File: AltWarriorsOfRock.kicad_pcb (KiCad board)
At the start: 2 copper layers, 35 x 90.5 mm, 17 parts, among them J1 Fret Board, J2 South Inputs

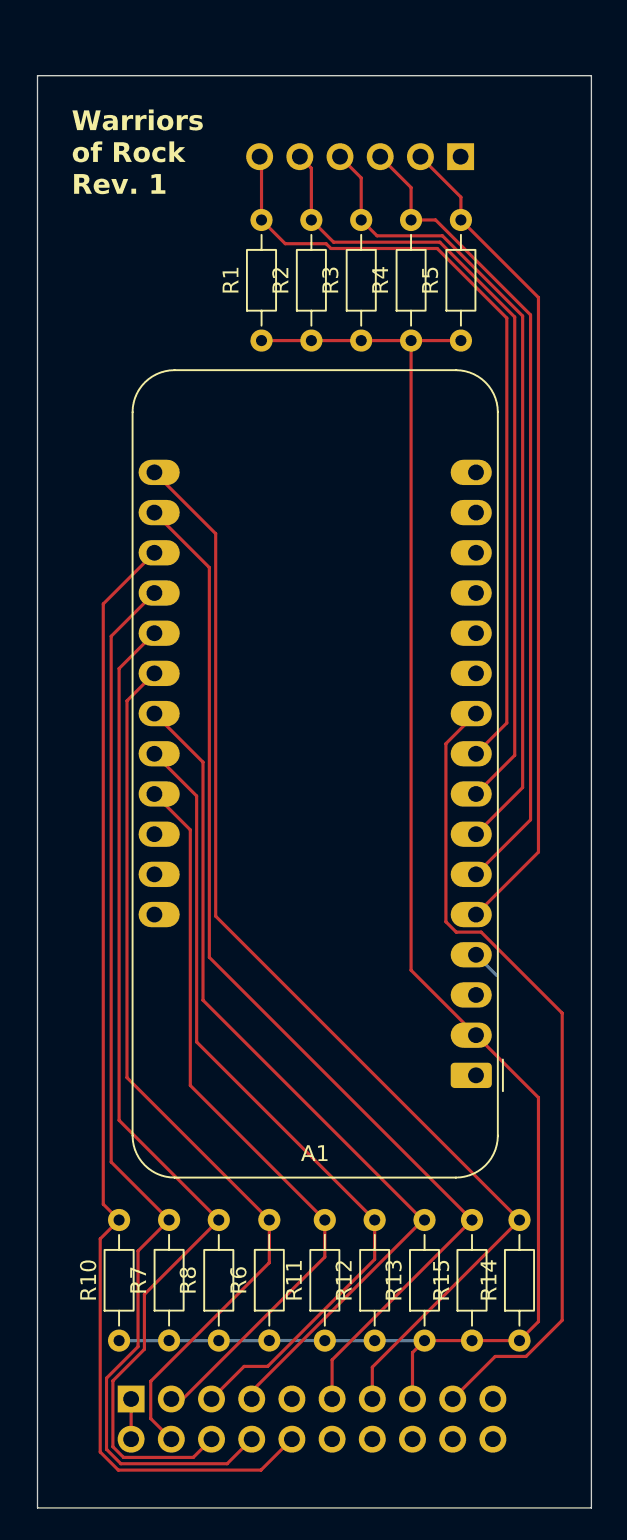
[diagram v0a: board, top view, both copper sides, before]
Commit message: Switch to ESP32-S3-WROOM-1 module; Use 5.1k for all pullups
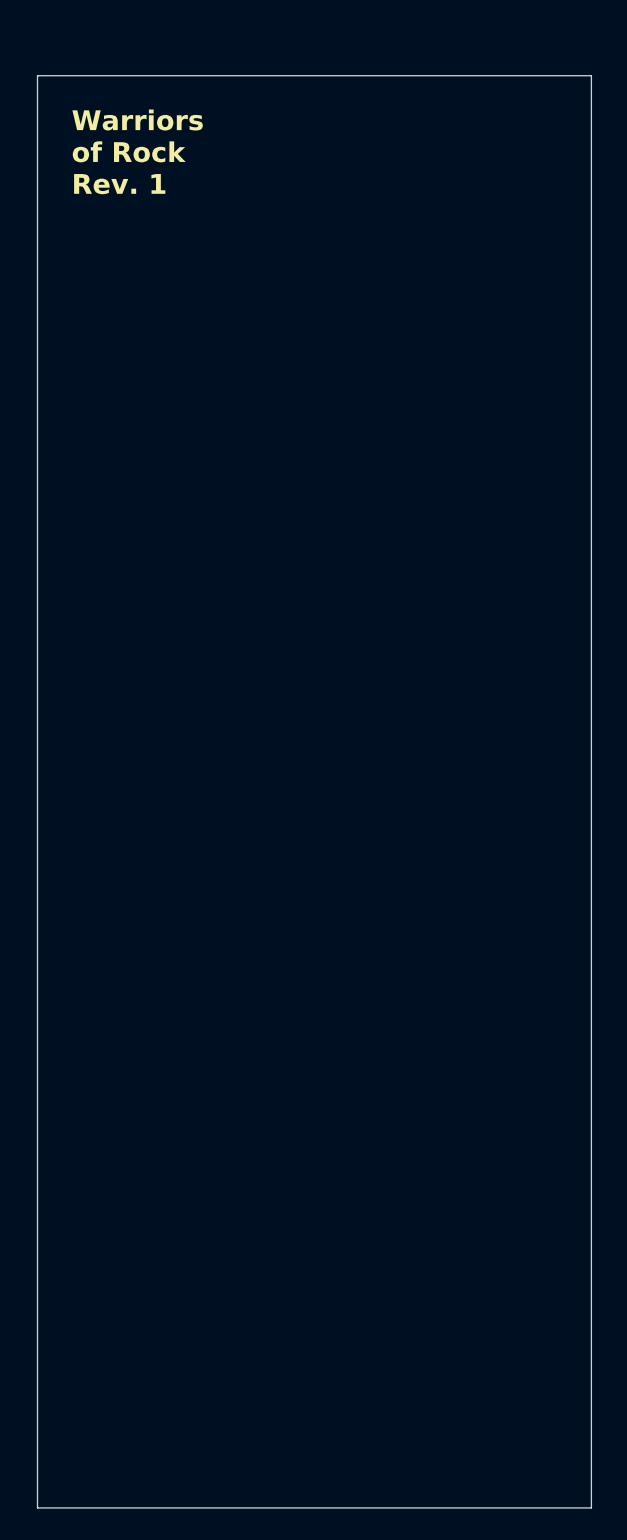
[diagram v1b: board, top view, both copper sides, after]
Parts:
- removed A1: Adafruit_Feather_Generic, Module:Adafruit_Feather
- removed J1: Fret Board, Connector_PinHeader_2.54mm:PinHeader_1x06_P2.54mm_Vertical
- removed J2: South Inputs, Library_ygaskh:PinHeader_2x10_P2.54mm_Vertical_TopBottom
- removed R1, R10, R11, R12, R13, R14, R15, R2, R3, R4, R5, R6, R7, R8: 1k, Resistor_THT:R_Axial_DIN0204_L3.6mm_D1.6mm_P7.62mm_Horizontal
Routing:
- net Wham_3V3: track 109.8 -> 0.00 mm
- net DPad_RIGHT: track 72.5 -> 0.00 mm
- net Strum_UP: track 72.0 -> 0.00 mm
- net Strum_DOWN: track 68.6 -> 0.00 mm
- net DPad_LEFT: track 68.6 -> 0.00 mm
- net DPad_DOWN: track 64.7 -> 0.00 mm
- net DPad_UP: track 56.5 -> 0.00 mm
- net Misc_Guide: track 55.6 -> 0.00 mm
- net Fret_O: track 53.0 -> 0.00 mm
- net Wham_Signal: track 52.1 -> 0.00 mm
- net Misc_Back: track 51.7 -> 0.00 mm
- net Fret_B: track 51.6 -> 0.00 mm
- net Fret_Y: track 51.2 -> 0.00 mm
- net Fret_R: track 50.8 -> 0.00 mm
- net Fret_G: track 50.5 -> 0.00 mm
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
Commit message: Draft 01 of PCB with WROOM module
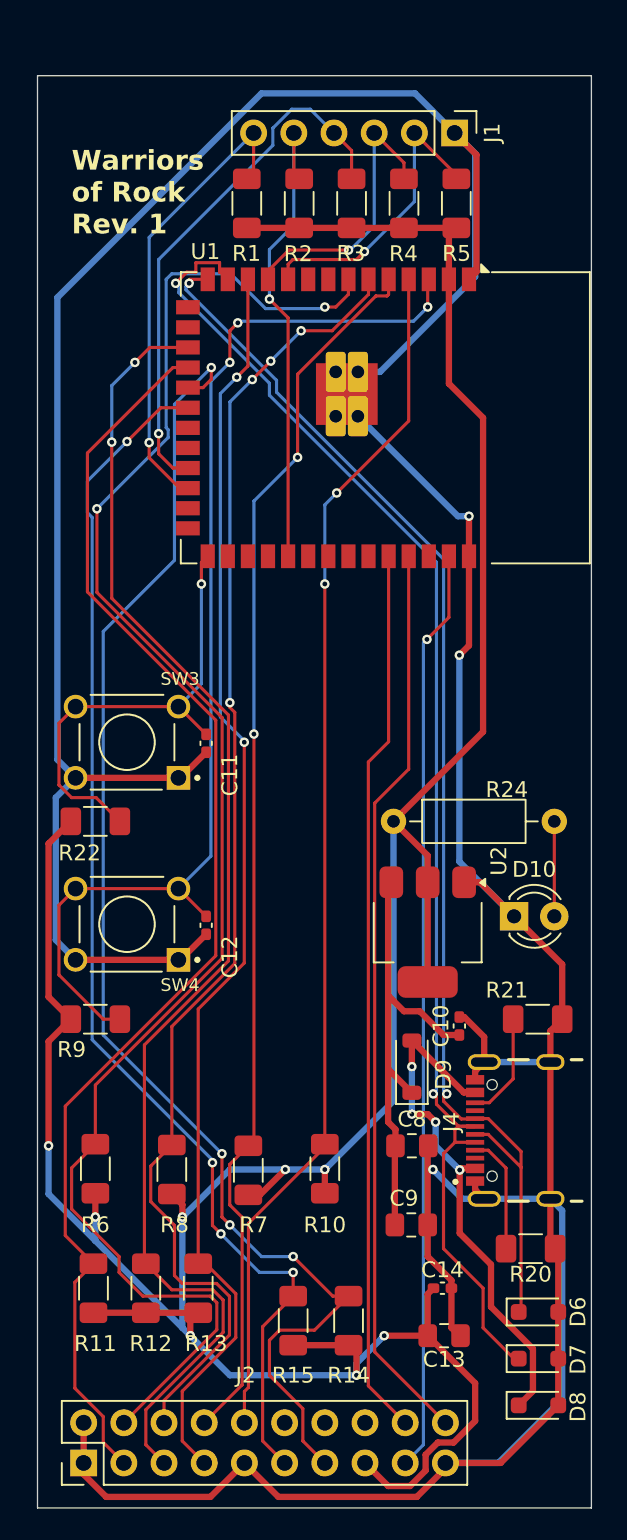
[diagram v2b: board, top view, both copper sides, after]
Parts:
- added C10: 0.1μ, Capacitor_SMD:C_0402_1005Metric_Pad0.74x0.62mm_HandSolder, F.Cu at (148.5, 113.4)
- added C11: 0.1μ, Capacitor_SMD:C_0402_1005Metric_Pad0.74x0.62mm_HandSolder, F.Cu at (132.5, 95.6)
- added C12: 0.1μ, Capacitor_SMD:C_0402_1005Metric_Pad0.74x0.62mm_HandSolder, F.Cu at (132.5, 107.1)
- added C13: 10μ, Capacitor_SMD:C_0805_2012Metric_Pad1.18x1.45mm_HandSolder, F.Cu at (147.5, 133.0)
- added C14: 0.1μ, Capacitor_SMD:C_0402_1005Metric_Pad0.74x0.62mm_HandSolder, F.Cu at (147.4, 130.0)
- added C8: 10μ, Capacitor_SMD:C_0805_2012Metric_Pad1.18x1.45mm_HandSolder, F.Cu at (145.5, 121.0)
- added C9: 10μ, Capacitor_SMD:C_0805_2012Metric_Pad1.18x1.45mm_HandSolder, F.Cu at (145.5, 126.0)
- added D10: PWRLED, LED_THT:LED_D3.0mm, F.Cu at (152.0, 106.5)
- added D6: D5V0L1B2WS-7, Diode_SMD:D_SOD-323_HandSoldering, F.Cu at (153.5, 131.5)
- added D7: D5V0L1B2WS-7, Diode_SMD:D_SOD-323_HandSoldering, F.Cu at (153.5, 134.4)
- added D8: D5V0L1B2WS-7, Diode_SMD:D_SOD-323_HandSoldering, F.Cu at (153.5, 137.4)
- added D9: 1N5819, Diode_SMD:D_SOD-123, F.Cu at (145.5, 116.0)
- added J1: Fret Board, Connector_PinHeader_2.54mm:PinHeader_1x06_P2.54mm_Vertical, F.Cu at (148.2, 57.0)
- added J2: South Inputs, Library_ygaskh:PinHeader_2x10_P2.54mm_Vertical_TopBottom, F.Cu at (124.8, 141.0)
- added J4: USB4930-00-A_REVA, Connector_3rd:GCT_USB4930-00-A_REVA, F.Cu at (154.3, 120.0)
- added R1: 5.1k, Resistor_SMD:R_1206_3216Metric_Pad1.30x1.75mm_HandSolder, F.Cu at (135.1, 61.5)
- added R10: 5.1k, Resistor_SMD:R_1206_3216Metric_Pad1.30x1.75mm_HandSolder, F.Cu at (140.0, 122.5)
- added R11: 5.1k, Resistor_SMD:R_1206_3216Metric_Pad1.30x1.75mm_HandSolder, F.Cu at (125.4, 130.0)
- added R12: 5.1k, Resistor_SMD:R_1206_3216Metric_Pad1.30x1.75mm_HandSolder, F.Cu at (128.7, 130.0)
- added R13: 5.1k, Resistor_SMD:R_1206_3216Metric_Pad1.30x1.75mm_HandSolder, F.Cu at (132.0, 130.0)
- added R14: 5.1k, Resistor_SMD:R_1206_3216Metric_Pad1.30x1.75mm_HandSolder, F.Cu at (141.5, 132.1)
- added R15: 5.1k, Resistor_SMD:R_1206_3216Metric_Pad1.30x1.75mm_HandSolder, F.Cu at (138.0, 132.1)
- added R2: 5.1k, Resistor_SMD:R_1206_3216Metric_Pad1.30x1.75mm_HandSolder, F.Cu at (138.4, 61.5)
- added R20: 5.1k, Resistor_SMD:R_1206_3216Metric_Pad1.30x1.75mm_HandSolder, F.Cu at (153.0, 127.5)
- added R21: 5.1k, Resistor_SMD:R_1206_3216Metric_Pad1.30x1.75mm_HandSolder, F.Cu at (153.4, 113.0)
- added R22: 5.1k, Resistor_SMD:R_1206_3216Metric_Pad1.30x1.75mm_HandSolder, F.Cu at (125.5, 100.5)
- added R24: 68, Resistor_THT:R_Axial_DIN0207_L6.3mm_D2.5mm_P10.16mm_Horizontal, F.Cu at (144.3, 100.5)
- added R3: 5.1k, Resistor_SMD:R_1206_3216Metric_Pad1.30x1.75mm_HandSolder, F.Cu at (141.7, 61.5)
- added R4: 5.1k, Resistor_SMD:R_1206_3216Metric_Pad1.30x1.75mm_HandSolder, F.Cu at (145.0, 61.5)
- added R5: 5.1k, Resistor_SMD:R_1206_3216Metric_Pad1.30x1.75mm_HandSolder, F.Cu at (148.3, 61.5)
- added R6: 5.1k, Resistor_SMD:R_1206_3216Metric_Pad1.30x1.75mm_HandSolder, F.Cu at (125.5, 122.5)
- added R7: 5.1k, Resistor_SMD:R_1206_3216Metric_Pad1.30x1.75mm_HandSolder, F.Cu at (135.2, 122.5)
- added R8: 5.1k, Resistor_SMD:R_1206_3216Metric_Pad1.30x1.75mm_HandSolder, F.Cu at (130.3, 122.5)
- added R9: 5.1k, Resistor_SMD:R_1206_3216Metric_Pad1.30x1.75mm_HandSolder, F.Cu at (125.5, 113.0)
- added SW3: 1825910-6, Switch_3rd:SW_1825910-6-4, F.Cu at (127.5, 95.5)
- added SW4: 1825910-6, Switch_3rd:SW_1825910-6-4, F.Cu at (127.5, 107.0)
- added U1: ESP32-S3-WROOM-1, RF_Module:ESP32-S3-WROOM-1, F.Cu at (143.8, 75.0)
- added U2: AMS1117-3.3, Package_TO_SOT_SMD:SOT-223-3_TabPin2, F.Cu at (146.5, 107.5)
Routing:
- net DPad_COM: track 0.00 -> 296.6 mm, vias 0 -> 3
- net Wham_3V3: track 0.00 -> 204.5 mm, vias 0 -> 8
- net DPad_UP: track 0.00 -> 104.0 mm, vias 0 -> 2
- net Strum_UP: track 0.00 -> 87.5 mm, vias 0 -> 4
- net USB_DN: track 0.00 -> 86.2 mm, vias 0 -> 2
- net Misc_Back: track 0.00 -> 85.2 mm, vias 0 -> 2
- net DPad_DOWN: track 0.00 -> 84.4 mm, vias 0 -> 4
- net Misc_Start: track 0.00 -> 82.2 mm
- net Misc_Guide: track 0.00 -> 80.6 mm, vias 0 -> 2
- net USB_DP: track 0.00 -> 80.3 mm, vias 0 -> 2
- net Strum_DOWN: track 0.00 -> 78.3 mm, vias 0 -> 4
- net DPad_LEFT: track 0.00 -> 78.1 mm, vias 0 -> 2
- net DPad_RIGHT: track 0.00 -> 76.5 mm, vias 0 -> 2
- net ESP_EN: track 0.00 -> 71.4 mm, vias 0 -> 3
- net Wham_Signal: track 0.00 -> 58.4 mm, vias 0 -> 1
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
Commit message: [WIP] Use surface-mount headers for south headers
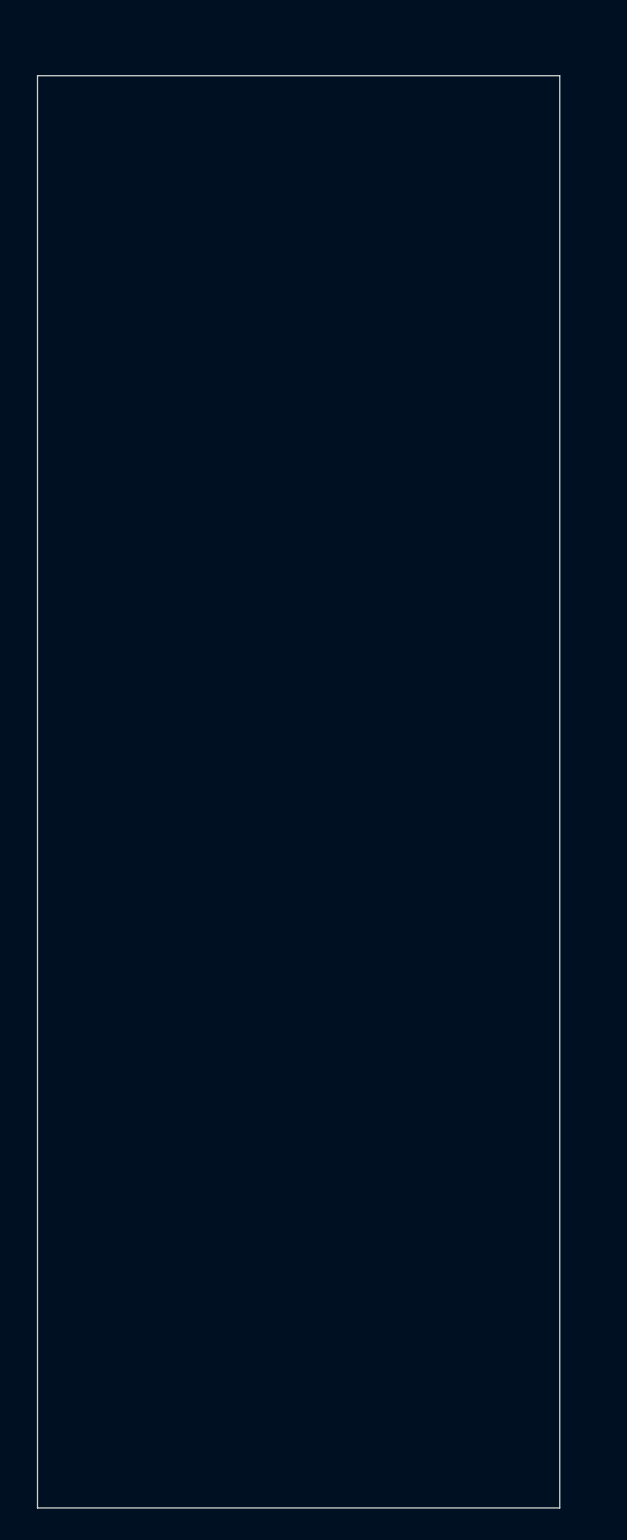
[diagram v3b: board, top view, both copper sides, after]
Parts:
- removed C10, C11, C12, C14: 0.1μ, Capacitor_SMD:C_0402_1005Metric_Pad0.74x0.62mm_HandSolder
- removed C13, C8, C9: 10μ, Capacitor_SMD:C_0805_2012Metric_Pad1.18x1.45mm_HandSolder
- removed D10: PWRLED, LED_THT:LED_D3.0mm
- removed D6, D7, D8: D5V0L1B2WS-7, Diode_SMD:D_SOD-323_HandSoldering
- removed D9: 1N5819, Diode_SMD:D_SOD-123
- removed J1: Fret Board, Connector_PinHeader_2.54mm:PinHeader_1x06_P2.54mm_Vertical
- removed J2: South Inputs, Library_ygaskh:PinHeader_2x10_P2.54mm_Vertical_TopBottom
- removed J4: USB4930-00-A_REVA, Connector_3rd:GCT_USB4930-00-A_REVA
- removed R1, R10, R11, R12, R13, R14, R15, R2, R20, R21, R22, R3, R4, R5, R6, R7, R8, R9: 5.1k, Resistor_SMD:R_1206_3216Metric_Pad1.30x1.75mm_HandSolder
- removed R24: 68, Resistor_THT:R_Axial_DIN0207_L6.3mm_D2.5mm_P10.16mm_Horizontal
- removed SW3, SW4: 1825910-6, Switch_3rd:SW_1825910-6-4
- removed U1: ESP32-S3-WROOM-1, RF_Module:ESP32-S3-WROOM-1
- removed U2: AMS1117-3.3, Package_TO_SOT_SMD:SOT-223-3_TabPin2
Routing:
- net DPad_COM: track 296.6 -> 0.00 mm, vias 3 -> 0
- net Wham_3V3: track 204.5 -> 0.00 mm, vias 8 -> 0
- net DPad_UP: track 104.0 -> 0.00 mm, vias 2 -> 0
- net Strum_UP: track 87.5 -> 0.00 mm, vias 4 -> 0
- net USB_DN: track 86.2 -> 0.00 mm, vias 2 -> 0
- net Misc_Back: track 85.2 -> 0.00 mm, vias 2 -> 0
- net DPad_DOWN: track 84.4 -> 0.00 mm, vias 4 -> 0
- net Misc_Start: track 82.2 -> 0.00 mm
- net Misc_Guide: track 80.6 -> 0.00 mm, vias 2 -> 0
- net USB_DP: track 80.3 -> 0.00 mm, vias 2 -> 0
- net Strum_DOWN: track 78.3 -> 0.00 mm, vias 4 -> 0
- net DPad_LEFT: track 78.1 -> 0.00 mm, vias 2 -> 0
- net DPad_RIGHT: track 76.5 -> 0.00 mm, vias 2 -> 0
- net ESP_EN: track 71.4 -> 0.00 mm, vias 3 -> 0
- net Wham_Signal: track 58.4 -> 0.00 mm, vias 1 -> 0
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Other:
- board size 35 x 90.5 mm -> 33 x 90.5 mm
- board text removed: "Warriors of Rock Rev. 1"

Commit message: Redo layout with USB-C port on the underside
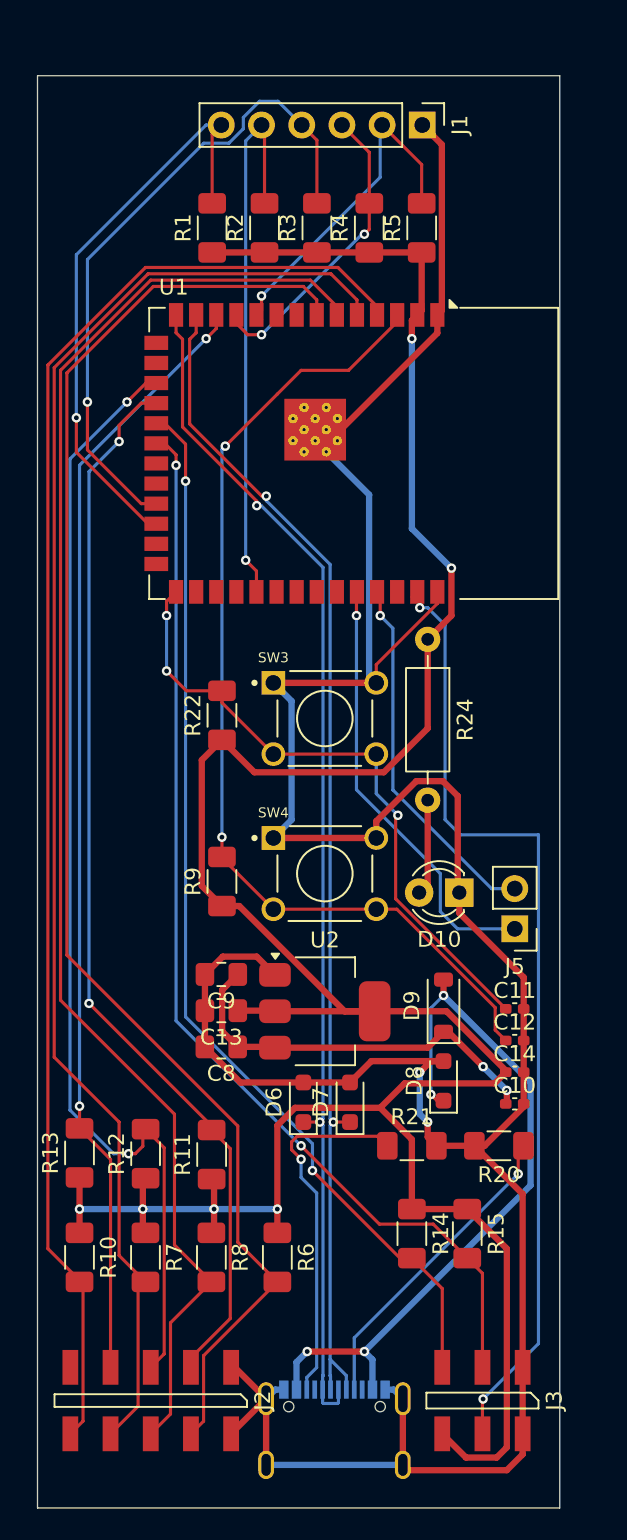
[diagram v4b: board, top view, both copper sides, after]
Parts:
- added C10: 0.1μ, Capacitor_SMD:C_0402_1005Metric_Pad0.74x0.62mm_HandSolder, F.Cu at (152.0, 118.3)
- added C11: 0.1μ, Capacitor_SMD:C_0402_1005Metric_Pad0.74x0.62mm_HandSolder, F.Cu at (152.0, 112.3)
- added C12: 0.1μ, Capacitor_SMD:C_0402_1005Metric_Pad0.74x0.62mm_HandSolder, F.Cu at (152.0, 114.3)
- added C13: 10μ, Capacitor_SMD:C_0805_2012Metric_Pad1.18x1.45mm_HandSolder, F.Cu at (133.5, 112.5)
- added C14: 0.1μ, Capacitor_SMD:C_0402_1005Metric_Pad0.74x0.62mm_HandSolder, F.Cu at (152.0, 116.3)
- added C8: 10μ, Capacitor_SMD:C_0805_2012Metric_Pad1.18x1.45mm_HandSolder, F.Cu at (133.5, 114.8)
- added C9: 10μ, Capacitor_SMD:C_0805_2012Metric_Pad1.18x1.45mm_HandSolder, F.Cu at (133.5, 110.2)
- added D10: PWRLED, LED_THT:LED_D3.0mm, F.Cu at (148.5, 105.0)
- added D6: D5V0L1B2WS-7, Diode_SMD:D_SOD-323_HandSoldering, F.Cu at (138.6, 118.2)
- added D7: D5V0L1B2WS-7, Diode_SMD:D_SOD-323_HandSoldering, F.Cu at (141.6, 118.2)
- added D8: D5V0L1B2WS-7, Diode_SMD:D_SOD-323_HandSoldering, F.Cu at (147.5, 116.9)
- added D9: 1N5819, Diode_SMD:D_SOD-123, F.Cu at (147.5, 112.2)
- added J1: Fret Board, Connector_PinHeader_2.54mm:PinHeader_1x06_P2.54mm_Vertical, F.Cu at (146.2, 56.5)
- added J2: PM20205HBDN, Connector_Metz_ygaskh:PM20205HBDN, F.Cu at (129.0, 137.1)
- added J3: PM20203HBDN, Connector_Metz_ygaskh:PM20203HBDN, F.Cu at (150.0, 137.1)
- added J4: USB4930-00-A_REVA, Connector_3rd:GCT_USB4930-00-A_REVA, B.Cu at (140.6, 141.2)
- added J5: Debug, Connector_PinHeader_2.54mm:PinHeader_1x02_P2.54mm_Vertical, F.Cu at (152.0, 107.3)
- added R1: 5.1k, Resistor_SMD:R_1206_3216Metric_Pad1.30x1.75mm_HandSolder, F.Cu at (132.9, 63.0)
- added R10: 5.1k, Resistor_SMD:R_1206_3216Metric_Pad1.30x1.75mm_HandSolder, F.Cu at (124.5, 128.1)
- added R11: 5.1k, Resistor_SMD:R_1206_3216Metric_Pad1.30x1.75mm_HandSolder, F.Cu at (132.8, 121.6)
- added R12: 5.1k, Resistor_SMD:R_1206_3216Metric_Pad1.30x1.75mm_HandSolder, F.Cu at (128.7, 121.5)
- added R13: 5.1k, Resistor_SMD:R_1206_3216Metric_Pad1.30x1.75mm_HandSolder, F.Cu at (124.5, 121.5)
- added R14: 5.1k, Resistor_SMD:R_1206_3216Metric_Pad1.30x1.75mm_HandSolder, F.Cu at (145.5, 126.5)
- added R15: 5.1k, Resistor_SMD:R_1206_3216Metric_Pad1.30x1.75mm_HandSolder, F.Cu at (149.0, 126.5)
- added R2: 5.1k, Resistor_SMD:R_1206_3216Metric_Pad1.30x1.75mm_HandSolder, F.Cu at (136.2, 63.0)
- added R20: 5.1k, Resistor_SMD:R_1206_3216Metric_Pad1.30x1.75mm_HandSolder, F.Cu at (151.0, 121.0)
- added R21: 5.1k, Resistor_SMD:R_1206_3216Metric_Pad1.30x1.75mm_HandSolder, F.Cu at (145.5, 121.0)
- added R22: 5.1k, Resistor_SMD:R_1206_3216Metric_Pad1.30x1.75mm_HandSolder, F.Cu at (133.5, 93.8)
- added R24: 68, Resistor_THT:R_Axial_DIN0207_L6.3mm_D2.5mm_P10.16mm_Horizontal, F.Cu at (146.5, 89.0)
- added R3: 5.1k, Resistor_SMD:R_1206_3216Metric_Pad1.30x1.75mm_HandSolder, F.Cu at (139.5, 63.0)
- added R4: 5.1k, Resistor_SMD:R_1206_3216Metric_Pad1.30x1.75mm_HandSolder, F.Cu at (142.8, 63.0)
- added R5: 5.1k, Resistor_SMD:R_1206_3216Metric_Pad1.30x1.75mm_HandSolder, F.Cu at (146.1, 63.0)
- added R6: 5.1k, Resistor_SMD:R_1206_3216Metric_Pad1.30x1.75mm_HandSolder, F.Cu at (137.0, 128.1)
- added R7: 5.1k, Resistor_SMD:R_1206_3216Metric_Pad1.30x1.75mm_HandSolder, F.Cu at (128.7, 128.1)
- added R8: 5.1k, Resistor_SMD:R_1206_3216Metric_Pad1.30x1.75mm_HandSolder, F.Cu at (132.8, 128.1)
- added R9: 5.1k, Resistor_SMD:R_1206_3216Metric_Pad1.30x1.75mm_HandSolder, F.Cu at (133.5, 104.3)
- added SW3: 1825910-6, Switch_3rd:SW_1825910-6-4, F.Cu at (140.0, 94.0)
- added SW4: 1825910-6, Switch_3rd:SW_1825910-6-4, F.Cu at (140.0, 103.8)
- added U1: ESP32-S3-WROOM-1, RF_Module:ESP32-S3-WROOM-1, F.Cu at (141.8, 77.2)
- added U2: AMS1117-3.3, Package_TO_SOT_SMD:SOT-223-3_TabPin2, F.Cu at (140.0, 112.5)
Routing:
- net DPad_COM: track 0.00 -> 195.4 mm, vias 0 -> 2
- net Wham_3V3: track 0.00 -> 180.3 mm, vias 0 -> 6
- net DPad_RIGHT: track 0.00 -> 94.8 mm
- net DPad_DOWN: track 0.00 -> 93.9 mm
- net DPad_LEFT: track 0.00 -> 93.8 mm
- net DPad_UP: track 0.00 -> 93.7 mm
- net USB_DP: track 0.00 -> 75.8 mm, vias 0 -> 2
- net USB_DN: track 0.00 -> 75.5 mm, vias 0 -> 2
- net Misc_Back: track 0.00 -> 71.6 mm, vias 0 -> 2
- net Misc_Guide: track 0.00 -> 71.1 mm, vias 0 -> 2
- net Strum_DOWN: track 0.00 -> 69.2 mm, vias 0 -> 2
- net Misc_Start: track 0.00 -> 68.0 mm, vias 0 -> 2
- net Strum_UP: track 0.00 -> 67.9 mm, vias 0 -> 2
- net ESP_EN: track 0.00 -> 64.2 mm, vias 0 -> 2
- net Wham_Signal: track 0.00 -> 61.5 mm, vias 0 -> 2
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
